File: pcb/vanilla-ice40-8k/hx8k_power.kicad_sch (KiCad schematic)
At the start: 37 parts, among them U1 ICE40HX8K-CT256

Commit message: [pcb][hx8k] set part numbers for 201 caps
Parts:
- C11, C13, C14, C16, C17, C18, C19, C21, C22, C23, C24, C26, C27, C28, C29, C3, C31, C32, C33, C34, C4, C5, C6, C7, C8, C9: Digi-Key Part Number (none) -> 490-14305-1-ND; LCSC Part # (none) -> C160831
- U1: Digi-Key Part Number (none) -> 220-1575-ND; LCSC Part # (none) -> C1521993
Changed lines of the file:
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@@
 			)
 		)
-		(property "LCSC Part #" ""
+		(property "LCSC Part #" "C160831"
 			(at 130.81 57.15 0)
 			(effects
@@
 			)
 		)
-		(property "Digi-Key Part Number" ""
+		(property "Digi-Key Part Number" "490-14305-1-ND"
 			(at 130.81 57.15 0)
 			(effects
@@
 			)
 		)
-		(property "LCSC Part #" ""
+		(property "LCSC Part #" "C160831"
 			(at 68.58 115.57 0)
 			(effects
@@
 			)
 		)
-		(property "Digi-Key Part Number" ""
+		(property "Digi-Key Part Number" "490-14305-1-ND"
 			(at 68.58 115.57 0)
 			(effects
@@
 			)
 		)
+		(property "LCSC Part #" "C1521993"
+			(at 119.38 102.87 0)
+			(effects
+				(font
+					(size 1.27 1.27)
+				)
+				(hide yes)
+			)
+		)
+		(property "Digi-Key Part Number" "220-1575-ND"
+			(at 119.38 102.87 0)
+			(effects
+				(font
+					(size 1.27 1.27)
+				)
+				(hide yes)
+			)
+		)
 		(pin "A9"
 		)
@@
 			)
 		)
-		(property "LCSC Part #" ""
+		(property "LCSC Part #" "C160831"
 			(at 100.33 48.26 0)
 			(effects
@@
 			)
 		)
-		(property "Digi-Key Part Number" ""
+		(property "Digi-Key Part Number" "490-14305-1-ND"
 			(at 100.33 48.26 0)
 			(effects
@@
 			)
 		)
-		(property "LCSC Part #" ""
+		(property "LCSC Part #" "C160831"
 			(at 68.58 86.36 0)
 			(effects
@@
 			)
 		)
-		(property "Digi-Key Part Number" ""
+		(property "Digi-Key Part Number" "490-14305-1-ND"
 			(at 68.58 86.36 0)
 			(effects
@@
 			)
 		)
-		(property "LCSC Part #" ""
+		(property "LCSC Part #" "C160831"
 			(at 182.88 86.36 0)
 			(effects
@@
 			)
 		)
-		(property "Digi-Key Part Number" ""
+		(property "Digi-Key Part Number" "490-14305-1-ND"
 			(at 182.88 86.36 0)
 			(effects
@@
 			)
 		)
-		(property "LCSC Part #" ""
+		(property "LCSC Part #" "C160831"
 			(at 48.26 86.36 0)
 			(effects
@@
 			)
 		)
-		(property "Digi-Key Part Number" ""
+		(property "Digi-Key Part Number" "490-14305-1-ND"
 			(at 48.26 86.36 0)
 			(effects
@@
 			)
 		)
-		(property "LCSC Part #" ""
+		(property "LCSC Part #" "C160831"
 			(at 153.67 49.53 0)
 			(effects
@@
 			)
 		)
-		(property "Digi-Key Part Number" ""
+		(property "Digi-Key Part Number" "490-14305-1-ND"
 			(at 153.67 49.53 0)
 			(effects
@@
 			)
 		)
-		(property "LCSC Part #" ""
+		(property "LCSC Part #" "C160831"
 			(at 58.42 48.26 0)
 			(effects
@@
 			)
 		)
-		(property "Digi-Key Part Number" ""
+		(property "Digi-Key Part Number" "490-14305-1-ND"
 			(at 58.42 48.26 0)
 			(effects
@@
 			)
 		)
-		(property "LCSC Part #" ""
+		(property "LCSC Part #" "C160831"
 			(at 58.42 115.57 0)
 			(effects
@@
 			)
 		)
-		(property "Digi-Key Part Number" ""
+		(property "Digi-Key Part Number" "490-14305-1-ND"
 			(at 58.42 115.57 0)
 			(effects
@@
 			)
 		)
-		(property "LCSC Part #" ""
+		(property "LCSC Part #" "C160831"
 			(at 90.17 48.26 0)
 			(effects
@@
 			)
 		)
-		(property "Digi-Key Part Number" ""
+		(property "Digi-Key Part Number" "490-14305-1-ND"
 			(at 90.17 48.26 0)
 			(effects
@@
 			)
 		)
-		(property "LCSC Part #" ""
+		(property "LCSC Part #" "C160831"
 			(at 58.42 86.36 0)
 			(effects
@@
 			)
 		)
-		(property "Digi-Key Part Number" ""
+		(property "Digi-Key Part Number" "490-14305-1-ND"
 			(at 58.42 86.36 0)
 			(effects
@@
 			)
 		)
-		(property "LCSC Part #" ""
+		(property "LCSC Part #" "C160831"
 			(at 78.74 86.36 0)
 			(effects
@@
 			)
 		)
-		(property "Digi-Key Part Number" ""
+		(property "Digi-Key Part Number" "490-14305-1-ND"
 			(at 78.74 86.36 0)
 			(effects
@@
 			)
 		)
-		(property "LCSC Part #" ""
+		(property "LCSC Part #" "C160831"
 			(at 176.53 49.53 0)
 			(effects
@@
 			)
 		)
-		(property "Digi-Key Part Number" ""
+		(property "Digi-Key Part Number" "490-14305-1-ND"
 			(at 176.53 49.53 0)
 			(effects
@@
 			)
 		)
-		(property "LCSC Part #" ""
+		(property "LCSC Part #" "C160831"
 			(at 80.01 48.26 0)
 			(effects
@@
 			)
 		)
-		(property "Digi-Key Part Number" ""
+		(property "Digi-Key Part Number" "490-14305-1-ND"
 			(at 80.01 48.26 0)
 			(effects
@@
 			)
 		)
-		(property "LCSC Part #" ""
+		(property "LCSC Part #" "C160831"
 			(at 97.79 66.04 0)
 			(effects
@@
 			)
 		)
-		(property "Digi-Key Part Number" ""
+		(property "Digi-Key Part Number" "490-14305-1-ND"
 			(at 97.79 66.04 0)
 			(effects
@@
 			)
 		)
-		(property "LCSC Part #" ""
+		(property "LCSC Part #" "C160831"
 			(at 48.26 115.57 0)
 			(effects
@@
 			)
 		)
-		(property "Digi-Key Part Number" ""
+		(property "Digi-Key Part Number" "490-14305-1-ND"
 			(at 48.26 115.57 0)
 			(effects
@@
 			)
 		)
-		(property "LCSC Part #" ""
+		(property "LCSC Part #" "C160831"
 			(at 193.04 115.57 0)
 			(effects
@@
 			)
 		)
-		(property "Digi-Key Part Number" ""
+		(property "Digi-Key Part Number" "490-14305-1-ND"
 			(at 193.04 115.57 0)
 			(effects
@@
 			)
 		)
-		(property "LCSC Part #" ""
+		(property "LCSC Part #" "C160831"
 			(at 172.72 86.36 0)
 			(effects
@@
 			)
 		)
-		(property "Digi-Key Part Number" ""
+		(property "Digi-Key Part Number" "490-14305-1-ND"
 			(at 172.72 86.36 0)
 			(effects
@@
 			)
 		)
-		(property "LCSC Part #" ""
+		(property "LCSC Part #" "C160831"
 			(at 172.72 115.57 0)
 			(effects
@@
 			)
 		)
-		(property "Digi-Key Part Number" ""
+		(property "Digi-Key Part Number" "490-14305-1-ND"
 			(at 172.72 115.57 0)
 			(effects
@@
 			)
 		)
-		(property "LCSC Part #" ""
+		(property "LCSC Part #" "C160831"
 			(at 78.74 115.57 0)
 			(effects
@@
 			)
 		)
-		(property "Digi-Key Part Number" ""
+		(property "Digi-Key Part Number" "490-14305-1-ND"
 			(at 78.74 115.57 0)
 			(effects
@@
 			)
 		)
-		(property "LCSC Part #" ""
+		(property "LCSC Part #" "C160831"
 			(at 182.88 115.57 0)
 			(effects
@@
 			)
 		)
-		(property "Digi-Key Part Number" ""
+		(property "Digi-Key Part Number" "490-14305-1-ND"
 			(at 182.88 115.57 0)
 			(effects
@@
 			)
 		)
-		(property "LCSC Part #" ""
+		(property "LCSC Part #" "C160831"
 			(at 203.2 86.36 0)
 			(effects
@@
 			)
 		)
-		(property "Digi-Key Part Number" ""
+		(property "Digi-Key Part Number" "490-14305-1-ND"
 			(at 203.2 86.36 0)
 			(effects
@@
 			)
 		)
-		(property "LCSC Part #" ""
+		(property "LCSC Part #" "C160831"
 			(at 203.2 115.57 0)
 			(effects
@@
 			)
 		)
-		(property "Digi-Key Part Number" ""
+		(property "Digi-Key Part Number" "490-14305-1-ND"
 			(at 203.2 115.57 0)
 			(effects
@@
 			)
 		)
-		(property "LCSC Part #" ""
+		(property "LCSC Part #" "C160831"
 			(at 69.85 48.26 0)
 			(effects
@@
 			)
 		)
-		(property "Digi-Key Part Number" ""
+		(property "Digi-Key Part Number" "490-14305-1-ND"
 			(at 69.85 48.26 0)
 			(effects
@@
 			)
 		)
-		(property "LCSC Part #" ""
+		(property "LCSC Part #" "C160831"
 			(at 193.04 86.36 0)
 			(effects
@@
 			)
 		)
-		(property "Digi-Key Part Number" ""
+		(property "Digi-Key Part Number" "490-14305-1-ND"
 			(at 193.04 86.36 0)
 			(effects
@@
 			)
 		)
-		(property "LCSC Part #" ""
+		(property "LCSC Part #" "C160831"
 			(at 48.26 48.26 0)
 			(effects
@@
 			)
 		)
-		(property "Digi-Key Part Number" ""
+		(property "Digi-Key Part Number" "490-14305-1-ND"
 			(at 48.26 48.26 0)
 			(effects

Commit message: [hx8k][pcb] place and route stackable connector on left
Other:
- title: (none) -> Vanilia Ice HX8K
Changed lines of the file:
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@@
 	(generator_version "8.0")
 	(paper "A4")
+	(title_block
+		(title "Vanilia Ice HX8K")
+		(rev "1.5.0")
+	)
 	(junction
 		(at 85.09 53.34)

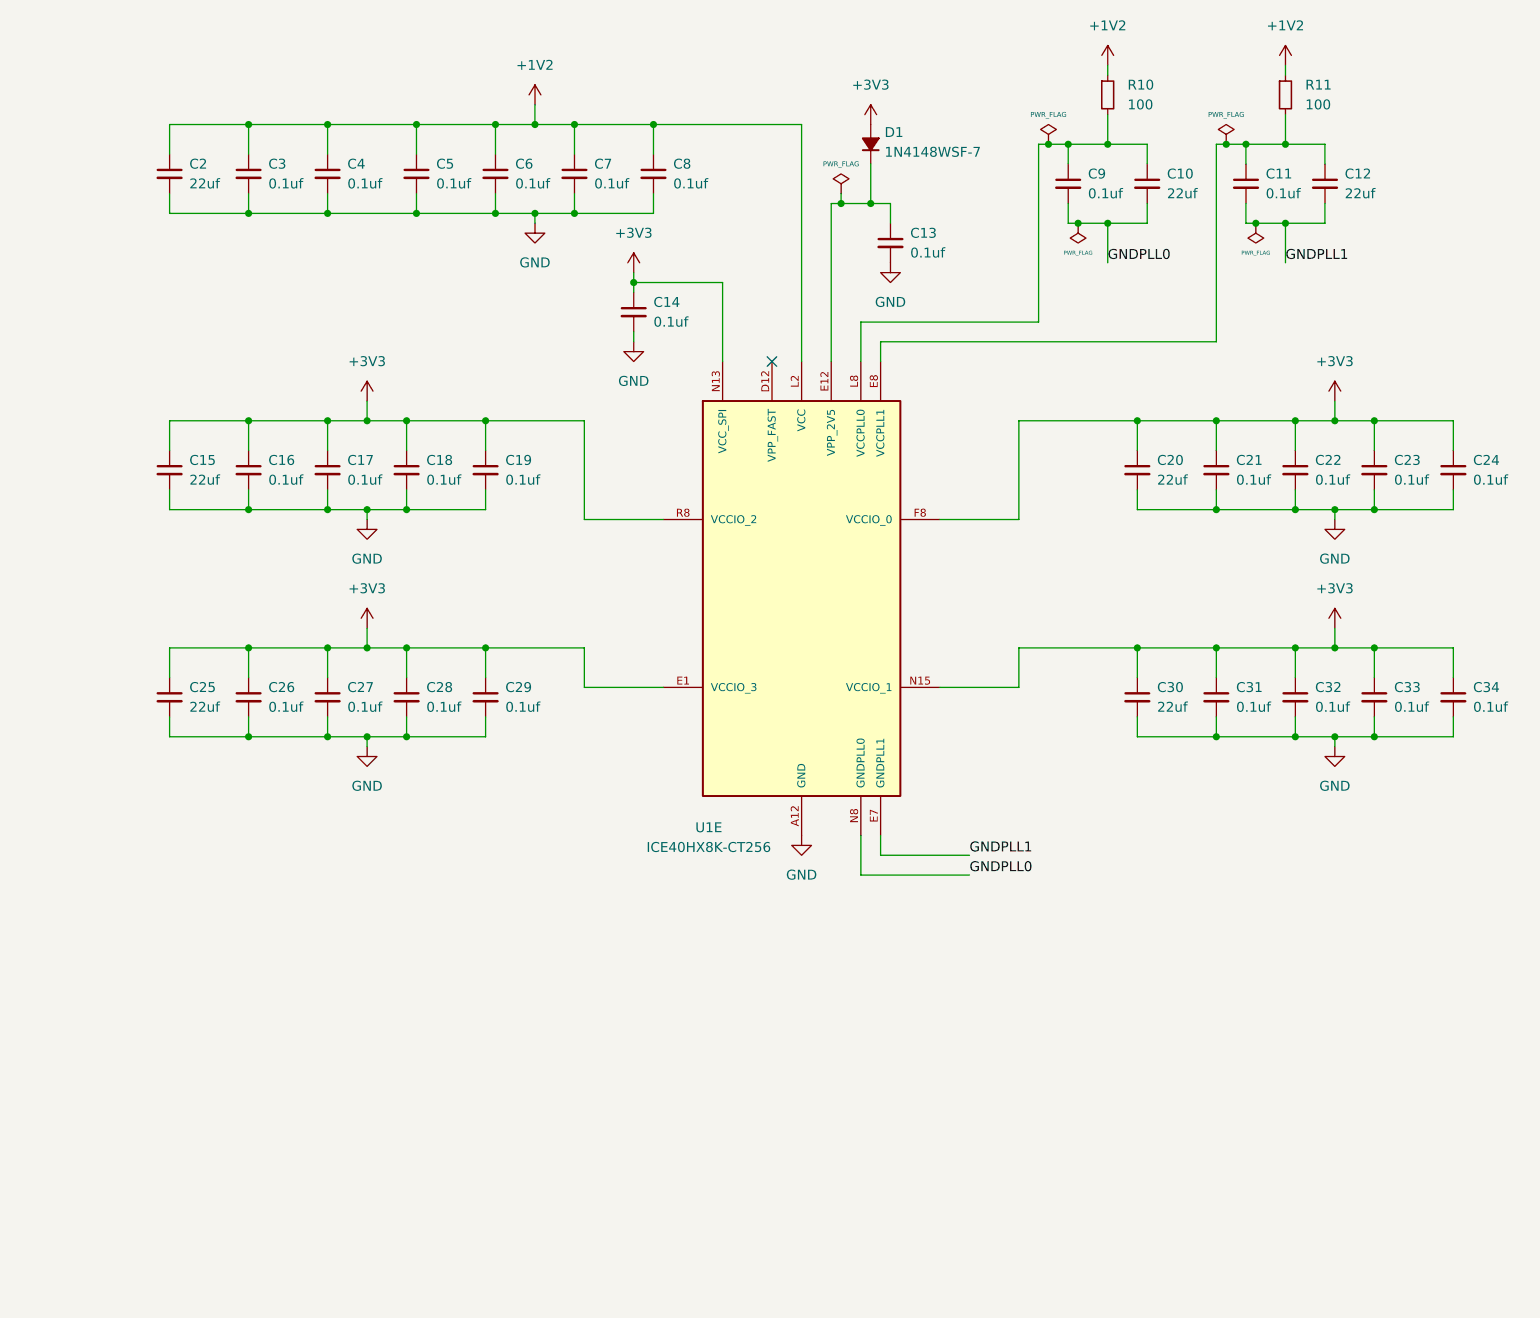
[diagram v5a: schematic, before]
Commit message: [hx8k][pcb] j1 and j2 mirroring fixed
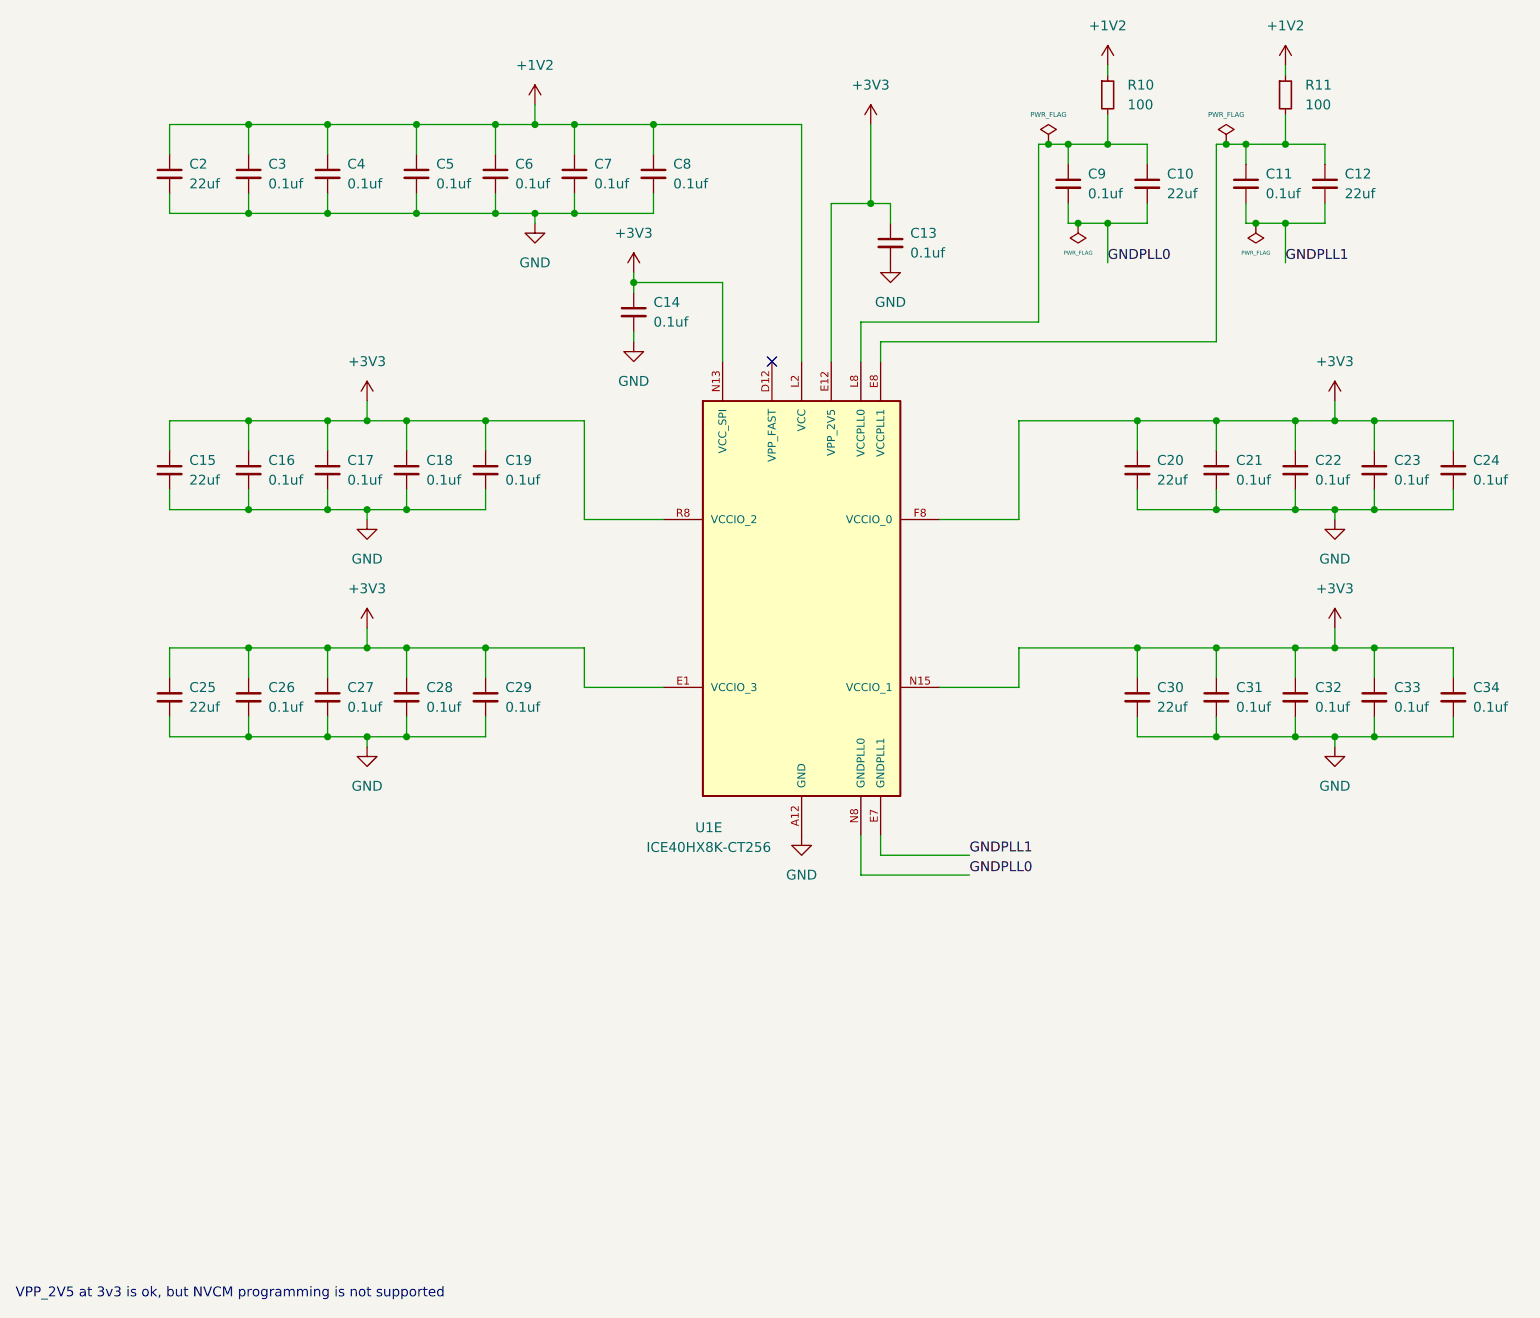
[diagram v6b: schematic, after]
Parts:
- removed D1: 1N4148WSF-7, Diode_SMD:D_SOD-323F, symbol Device:D_Small_Filled
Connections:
- net +3V3: now also C13.1, U1.E12 (VPP_2V5)
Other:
- note added: "VPP_2V5 at 3v3 is ok, but NVCM programming is not supported"
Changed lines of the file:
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@@
 		(rev "1.5.0")
 	)
+	(text "VPP_2V5 at 3v3 is ok, but NVCM programming is not supported"
+		(exclude_from_sim no)
+		(at 18.288 192.278 0)
+		(effects
+			(font
+				(size 1.27 1.27)
+			)
+			(justify left)
+		)
+	)
 	(junction
 		(at 85.09 53.34)
@@
 	)
 	(junction
-		(at 124.46 52.07)
-		(diameter 0)
-		(color 0 0 0 0)
-	)
-	(junction
 		(at 100.33 41.91)
 		(diameter 0)
@@
 	(wire
 		(pts
+			(xy 123.19 52.07) (xy 128.27 52.07)
+		)
+		(stroke
+			(width 0)
+			(type default)
+		)
+	)
+	(wire
+		(pts
 			(xy 149.86 67.31) (xy 149.86 44.45)
 		)
@@
 	(wire
 		(pts
-			(xy 128.27 52.07) (xy 128.27 46.99)
-		)
-		(stroke
-			(width 0)
-			(type default)
-		)
-	)
-	(wire
-		(pts
 			(xy 130.81 54.61) (xy 130.81 52.07)
 		)
@@
 	(wire
 		(pts
-			(xy 123.19 52.07) (xy 124.46 52.07)
-		)
-		(stroke
-			(width 0)
-			(type default)
-		)
-	)
-	(wire
-		(pts
 			(xy 68.58 88.9) (xy 68.58 91.44)
 		)
@@
 	(wire
 		(pts
-			(xy 124.46 50.8) (xy 124.46 52.07)
-		)
-		(stroke
-			(width 0)
-			(type default)
-		)
-	)
-	(wire
-		(pts
 			(xy 58.42 41.91) (xy 69.85 41.91)
 		)
@@
 	(wire
 		(pts
-			(xy 124.46 52.07) (xy 128.27 52.07)
-		)
-		(stroke
-			(width 0)
-			(type default)
-		)
-	)
-	(wire
-		(pts
 			(xy 182.88 80.01) (xy 182.88 83.82)
 		)
@@
 	(wire
 		(pts
+			(xy 128.27 41.91) (xy 128.27 52.07)
+		)
+		(stroke
+			(width 0)
+			(type default)
+		)
+	)
+	(wire
+		(pts
 			(xy 176.53 54.61) (xy 176.53 52.07)
 		)
@@
 	)
 	(symbol
-		(lib_id "Device:D_Small_Filled")
-		(at 128.27 44.45 90)
-		(unit 1)
-		(exclude_from_sim no)
-		(in_bom yes)
-		(on_board yes)
-		(dnp no)
-		(property "Reference" "D1"
-			(at 130.048 42.926 90)
-			(effects
-				(font
-					(size 1.27 1.27)
-				)
-				(justify right)
-			)
-		)
-		(property "Value" "1N4148WSF-7"
-			(at 130.048 45.466 90)
-			(effects
-				(font
-					(size 1.27 1.27)
-				)
-				(justify right)
-			)
-		)
-		(property "Footprint" "Diode_SMD:D_SOD-323F"
-			(at 128.27 44.45 90)
-			(effects
-				(font
-					(size 1.27 1.27)
-				)
-				(hide yes)
-			)
-		)
-		(property "Datasheet" "~"
-			(at 128.27 44.45 90)
-			(effects
-				(font
-					(size 1.27 1.27)
-				)
-				(hide yes)
-			)
-		)
-		(property "Description" "Diode, small symbol, filled shape"
-			(at 128.27 44.45 0)
-			(effects
-				(font
-					(size 1.27 1.27)
-				)
-				(hide yes)
-			)
-		)
-		(property "Sim.Device" "D"
-			(at 128.27 44.45 0)
-			(effects
-				(font
-					(size 1.27 1.27)
-				)
-				(hide yes)
-			)
-		)
-		(property "Sim.Pins" "1=K 2=A"
-			(at 128.27 44.45 0)
-			(effects
-				(font
-					(size 1.27 1.27)
-				)
-				(hide yes)
-			)
-		)
-		(property "LCSC Part #" "C119617"
-			(at 128.27 44.45 0)
-			(effects
-				(font
-					(size 1.27 1.27)
-				)
-				(hide yes)
-			)
-		)
-		(property "JLCPCB Rotation Offset" ""
-			(at 128.27 44.45 0)
-			(effects
-				(font
-					(size 1.27 1.27)
-				)
-				(hide yes)
-			)
-		)
-		(property "Digi-Key Part Number" "1N4148WSF-7DICT-ND"
-			(at 128.27 44.45 0)
-			(effects
-				(font
-					(size 1.27 1.27)
-				)
-				(hide yes)
-			)
-		)
-		(pin "2"
-		)
-		(pin "1"
-		)
-		(instances
-			(project "vanilla-ice40-8k"
-				(path "/6fdfbf4b-014a-4077-8dc3-7ce5ecaf5fe5/8fa8b499-bf6e-428e-9b7b-1dd20539af7f"
-					(reference "D1")
-					(unit 1)
-				)
-			)
-		)
-	)
-	(symbol
 		(lib_id "Device:C_Small")
 		(at 172.72 86.36 0)
@@
 					(unit 1)
 				)
-			)
-		)
-	)
-	(symbol
-		(lib_id "power:PWR_FLAG")
-		(at 124.46 50.8 0)
-		(unit 1)
-		(exclude_from_sim no)
-		(in_bom yes)
-		(on_board yes)
-		(dnp no)
-		(property "Reference" "#FLG03"
-			(at 124.46 48.895 0)
-			(effects
-				(font
-					(size 1.27 1.27)
-				)
-				(hide yes)
-			)
-		)
-		(property "Value" "PWR_FLAG"
-			(at 124.46 46.99 0)
-			(effects
-				(font
-					(size 0.635 0.635)
-				)
-			)
-		)
-		(property "Footprint" ""
-			(at 124.46 50.8 0)
-			(effects
-				(font
-					(size 1.27 1.27)
-				)
-				(hide yes)
-			)
-		)
-		(property "Datasheet" "~"
-			(at 124.46 50.8 0)
-			(effects
-				(font
-					(size 1.27 1.27)
-				)
-				(hide yes)
-			)
-		)
-		(property "Description" "Special symbol for telling ERC where power comes from"
-			(at 124.46 50.8 0)
-			(effects
-				(font
-					(size 1.27 1.27)
-				)
-				(hide yes)
-			)
-		)
-		(pin "1"
-		)
-		(instances
-			(project "vanilla-ice40-8k"
-				(path "/6fdfbf4b-014a-4077-8dc3-7ce5ecaf5fe5/8fa8b499-bf6e-428e-9b7b-1dd20539af7f"
-					(reference "#FLG03")
-					(unit 1)
-				)

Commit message: [hx8k][pcb] move top level to use symbol lib
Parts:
- C11, C13, C14, C16, C17, C18, C19, C21, C22, C23, C24, C26, C27, C28, C29, C3, C31, C32, C33, C34, C4, C5, C6, C7, C8, C9: symbol Device:C_Small -> !Misc:C_0.1uf_0201; LCSC Part # C160831 -> C160831
- R10, R11: symbol Device:R_Small -> !Misc:R_2.2K_0603
